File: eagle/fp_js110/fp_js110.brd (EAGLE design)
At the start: 95 x 24.7 mm, 2 parts

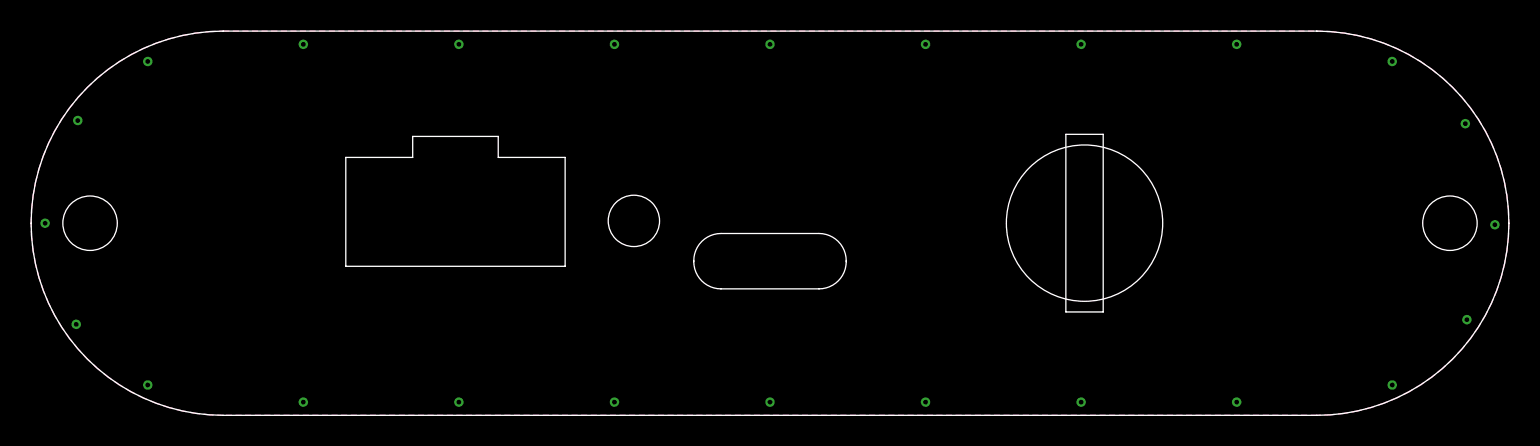
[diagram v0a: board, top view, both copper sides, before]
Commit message: Updates for JS220 first production build.
* Updated back panel for production build.
  * Increased USB hole size by 0.2 mm in left, right, and up directions
  * Bumped rev from C to D.
* Added additional boards:
  * fb_usb2_ba: USB 2.0 B/A connector
  * fp_bnc: BNC & 0.1" headers
  * fp_js110: Safety banana jacks configured like the JS110.
  * fp_baseline: Starting point for creating new boards in Eagle.
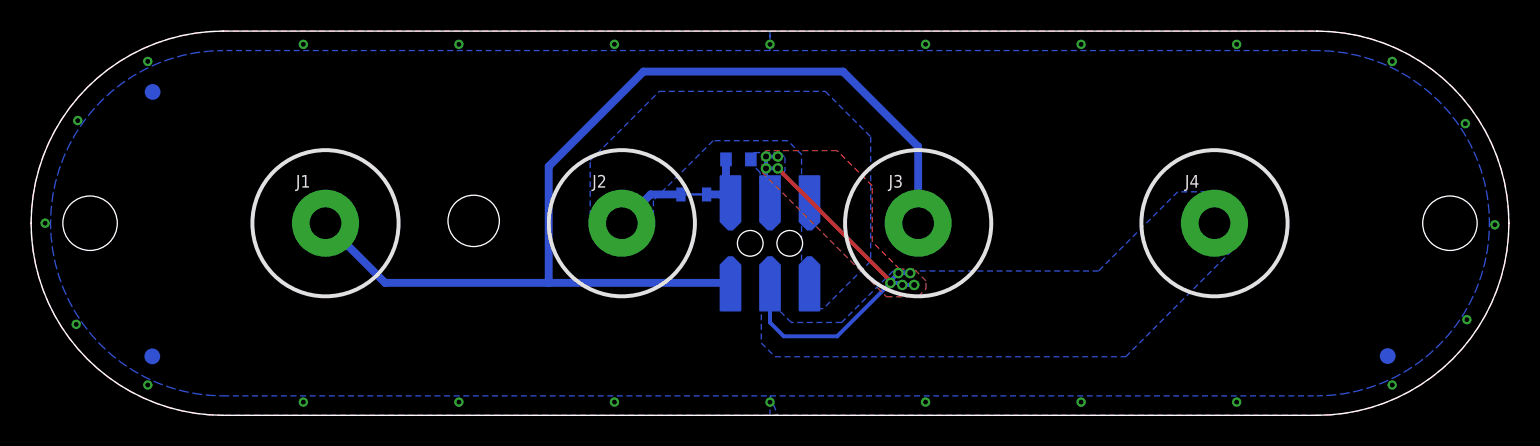
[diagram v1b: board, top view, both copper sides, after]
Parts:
- added FUD1, FUD2, FUD3: FIDUCIAL_1MM, jetperch:FIDUCIAL_1MM_2MM
- added J1, J3: CT3149-0, jetperch:CT3149
- added J2, J4: CT3149-2, jetperch:CT3149
- added J5: TSM-103-01-S-DV-A, jetperch:CONN_0.1_3X2_MSA
- added J6: (no value), jetperch:J0603
- added R1: 0, jetperch:0603
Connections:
- new net I+: J2.A, J5.1, J5.2, J6.2
- new net I-: J4.A, J5.3, J5.4, R1.2
- new net V+: J5.6, J6.1, R1.1
- new net V-: J1.A, J3.A, J5.5
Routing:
- net V-: track 0.00 -> 68.3 mm
- net I-: track 0.00 -> 30.3 mm, vias 0 -> 9
- net I+: track 0.00 -> 4.57 mm
- net V+: track 0.00 -> 4.26 mm
- added copper zone on layer 16, net I+
- added copper zone on layer 1, net I-
- added copper zone on layer 16, net I-
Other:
- outline, holes or cut-outs redrawn
- board text added: "+"
- board text added: "-"
- board text added: "2x holes"
- board text added: "IN"
- board text added: "Isolated ±48V max to USB ground"
- board text added: "JS220_fp_js110_pcb_a JS220 Safety Banana Jack, JS110-compatible Front Panel, Rev A 2022 Jetperch LLC"
- board text added: "OUT"
- board text added: "Sensor Status"
- board text added: "±15V ±3A"
- board text removed: "Controller Status"
- board text removed: "GPIO"
- board text removed: "GPIO and trigger are referenced to USB ground"
- board text removed: "OUT0 GND IN2 IN0 Vref"
- board text removed: "OUT1 GND IN3 IN1 GND"
- board text removed: "Out: 3.3V, 50 Ω In: TTL & 3.3V compatible"
- board text removed: "Trigger"
- board text removed: "USB"
- board text removed: "js220_ep_pcb_revC JS220 End Panel, Rev D 2022 Jetperch LLC"
